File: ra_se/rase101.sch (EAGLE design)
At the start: 32 parts, among them IC1 74HC14D, IC2 24LC08BSN, X1 MAB5WH, X12 LED_01, X2 22-23-2041, X3 MAB5WH

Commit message: ra_se evolve
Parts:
- removed R10: 3k3, rcl:R-EU_M1206
- removed X5, X6: (no value), con-molex:KK-156-3
- added R11: 10k, rcl:R-EU_M1206
- X4: device con-molex:KK-156-3 -> con-molex:KK-156-2
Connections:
- net BTTN_GLOBALSTART renamed BTTN_03
- net BTTN_START_REQST renamed BTTN_01
- net BTTN_STOP_REQST renamed BTTN_02
- net UART1_TX renamed UART1_TX_MAX_I
- removed net INMI_SH: IC1C.O, X5-1.S, X6-1.S
- removed net MAX_O: U$2.RO, X6-3.S
- removed net N$10: U$1.PA10, X6-2.S
- removed net N$11: U$2.DE, U$2.RE, X4-2.S
- removed net N$7: R8.2, X5-2.S
- new net BC2812: IC1A.O, X4-1.S
- new net N$9: IC1A.I, IC1F.O
- new net RS485DIRECT: R11.2, U$1.PB4, U$2.DE, U$2.RE
- new net SPI1_MOSI: IC1F.I, U$1.PA7
- new net UART1_RX_MAX_O: U$1.PA10, U$2.RO
- net +3V3: now also R3.1, R6.1, X2-2.S
- net +5V: now also R11.1; no longer R10.1, R3.1, R6.1, X2-2.S, X4-1.S
- net ENCODER0: now also IC1D.I
- net ENCODER1: now also IC1E.I
- net GND: now also X4-2.S; no longer X4-3.S
- net INMI: now also IC1B.I
- net TIC_RESET: no longer R10.2
- net UART2_RX: now also IC1C.O
- net UART2_TX: now also R8.2; no longer X5-3.S
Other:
- moved on the sheet: IC1A, IC1B, IC1C, IC1D, IC1E, IC1F, IC1P, R3, R6, U$2, X10-1, X10-2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

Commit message: fix
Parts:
- added R10: 10k, rcl:R-EU_M1206
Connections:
- net +5V: now also R10.1
- net UART1_TX_MAX_I: now also R10.2
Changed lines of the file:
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@@
 <part name="GND7" library="supply1" deviceset="GND" device=""/>
 <part name="+3V1" library="supply1" deviceset="+3V3" device=""/>
+<part name="R10" library="rcl" deviceset="R-EU_" device="M1206" value="10k"/>
+<part name="P+2" library="supply1" deviceset="+5V" device=""/>
 </parts>
 <sheets>
@@
 <instance part="GND7" gate="1" x="289.56" y="71.12"/>
 <instance part="+3V1" gate="G$1" x="160.02" y="83.82"/>
+<instance part="R10" gate="G$1" x="109.22" y="101.6" rot="R270"/>
+<instance part="P+2" gate="1" x="109.22" y="111.76"/>
 </instances>
 <busses>
@@
 <segment>
 <pinref part="U$1" gate="G$1" pin="PA10"/>
-<wire x1="76.2" y1="73.66" x2="83.82" y2="73.66" width="0.1524" layer="91"/>
-<label x="83.82" y="73.66" size="1.27" layer="95" xref="yes"/>
+<wire x1="76.2" y1="73.66" x2="81.28" y2="73.66" width="0.1524" layer="91"/>
+<label x="114.3" y="73.66" size="1.27" layer="95" xref="yes"/>
+<wire x1="83.82" y1="73.66" x2="114.3" y2="73.66" width="0.1524" layer="91"/>
+<wire x1="81.28" y1="73.66" x2="83.82" y2="73.66" width="0.1524" layer="91"/>
 </segment>
 </net>
@@
 <pinref part="P+11" gate="1" pin="+5V"/>
 <wire x1="101.6" y1="99.06" x2="101.6" y2="101.6" width="0.1524" layer="91"/>
+</segment>
+<segment>
+<pinref part="P+2" gate="1" pin="+5V"/>
+<pinref part="R10" gate="G$1" pin="1"/>
+<wire x1="109.22" y1="109.22" x2="109.22" y2="106.68" width="0.1524" layer="91"/>
 </segment>
 </net>
@@
 <segment>
 <pinref part="U$1" gate="G$1" pin="PB3"/>
-<wire x1="76.2" y1="83.82" x2="109.22" y2="83.82" width="0.1524" layer="91"/>
-<label x="109.22" y="83.82" size="1.27" layer="95" xref="yes"/>
+<wire x1="76.2" y1="83.82" x2="114.3" y2="83.82" width="0.1524" layer="91"/>
+<label x="114.3" y="83.82" size="1.27" layer="95" xref="yes"/>
 </segment>
 </net>
@@
 <pinref part="R11" gate="G$1" pin="2"/>
 <wire x1="101.6" y1="86.36" x2="101.6" y2="88.9" width="0.1524" layer="91"/>
-<wire x1="101.6" y1="86.36" x2="109.22" y2="86.36" width="0.1524" layer="91"/>
+<wire x1="101.6" y1="86.36" x2="114.3" y2="86.36" width="0.1524" layer="91"/>
 <junction x="101.6" y="86.36"/>
-<label x="109.22" y="86.36" size="1.27" layer="95" xref="yes"/>
+<label x="114.3" y="86.36" size="1.27" layer="95" xref="yes"/>
 </segment>
 <segment>
@@
 <segment>
 <pinref part="U$1" gate="G$1" pin="PA9"/>
-<wire x1="76.2" y1="71.12" x2="83.82" y2="71.12" width="0.1524" layer="91"/>
-<label x="83.82" y="71.12" size="1.27" layer="95" xref="yes"/>
-</segment>
-<segment>
+<wire x1="76.2" y1="71.12" x2="109.22" y2="71.12" width="0.1524" layer="91"/>
+<label x="114.3" y="71.12" size="1.27" layer="95" xref="yes"/>
+<pinref part="R10" gate="G$1" pin="2"/>
+<wire x1="109.22" y1="71.12" x2="114.3" y2="71.12" width="0.1524" layer="91"/>
+<wire x1="109.22" y1="96.52" x2="109.22" y2="71.12" width="0.1524" layer="91"/>
+<junction x="109.22" y="71.12"/>
+</segment>
+<segment>

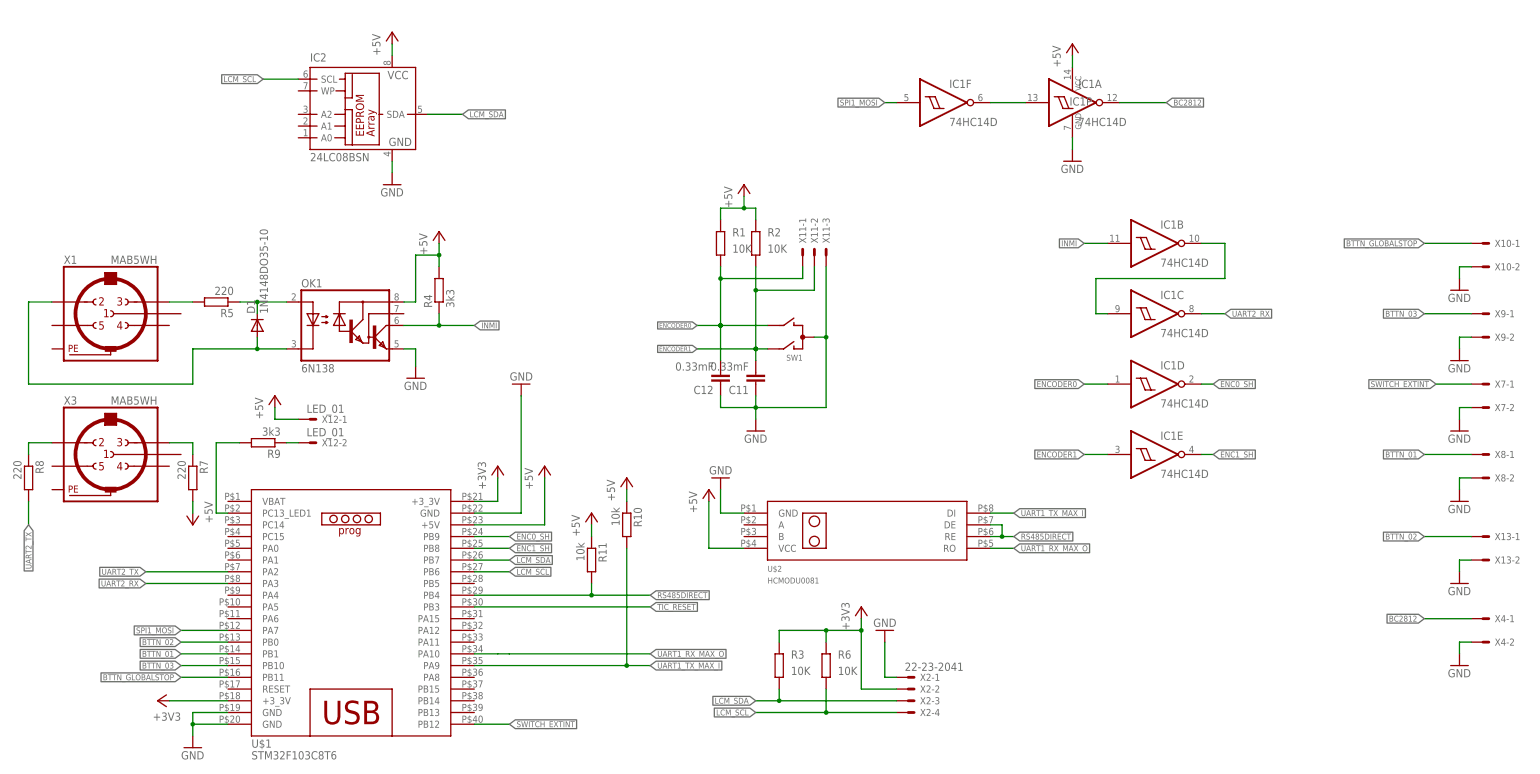
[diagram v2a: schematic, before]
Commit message: oled and other
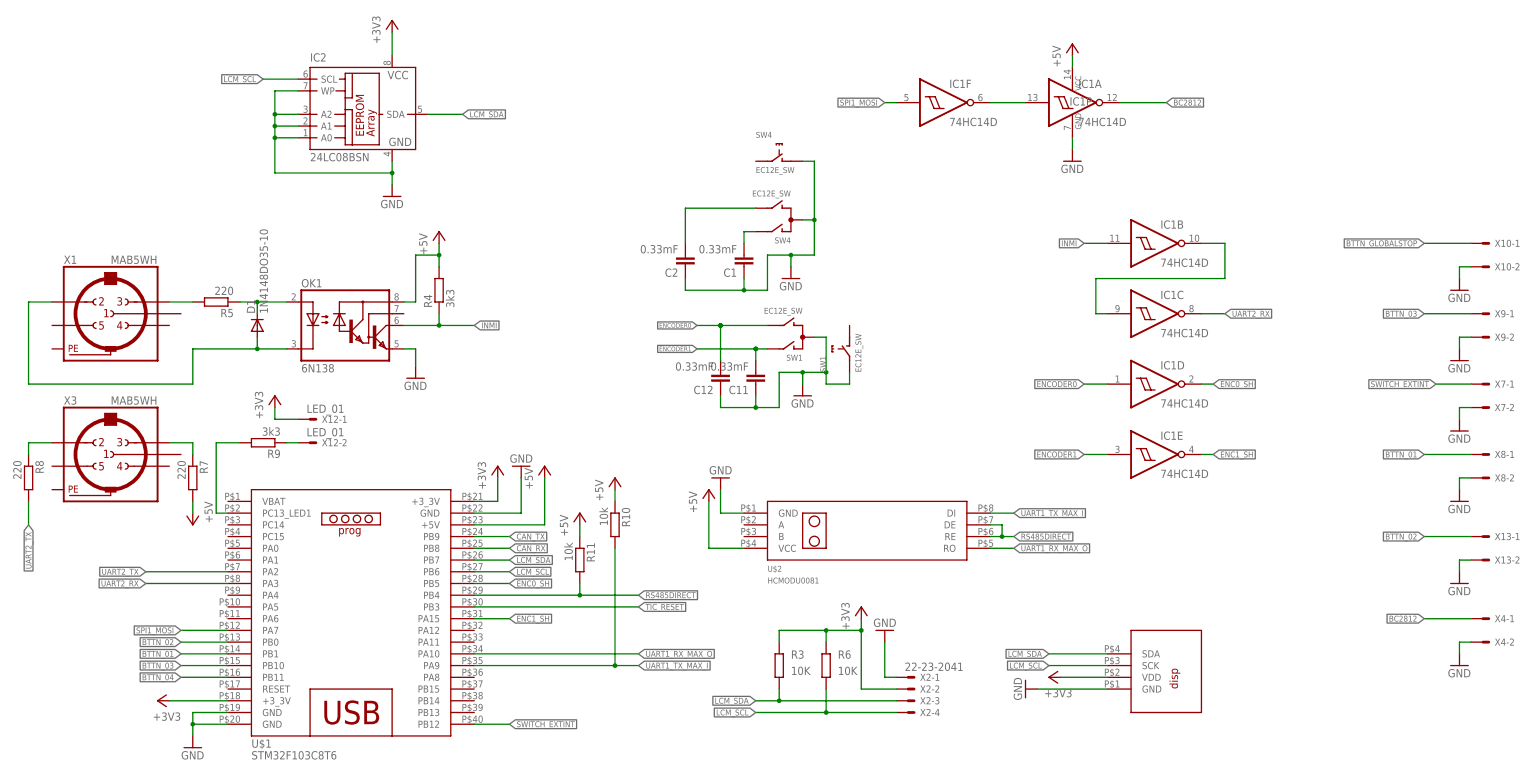
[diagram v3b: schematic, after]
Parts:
- removed R1, R2: 10K, quantum-sensor:R-R1206
- removed X11: (no value), con-molex:KK-156-3
- added C1, C2: 0.33mF, quantum-sensor:C-1206
- added SW4: EC12E_SW, switch-alps:EC12E_SW
- added U$3: OLED_0.96, kolio_oled:OLED_0.96
- SW1: value (none) -> EC12E_SW
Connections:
- new net BTTN_04: U$1.PB11
- new net CAN_RX: U$1.PB8
- new net CAN_TX: U$1.PB9
- new net N$13: C1.2, SW4G$1.A
- new net N$14: C2.2, SW4G$1.B
- net +3V3: now also IC2.VCC, U$3.VDD, X12-1.S
- net +5V: no longer IC2.VCC, R1.1, R2.1, X12-1.S
- net BTTN_GLOBALSTOP: no longer U$1.PB11
- net ENC0_SH: now also U$1.PB5; no longer U$1.PB9
- net ENC1_SH: now also U$1.PA15; no longer U$1.PB8
- net ENCODER0: no longer R1.2, X11-1.S
- net ENCODER1: no longer R2.2, X11-2.S
- net GND: now also C1.1, C2.1, IC2.A0, IC2.A1, IC2.A2, IC2.WP, SW1G$2.2, SW4G$1.C, SW4G$2.1, U$3.GND; no longer X11-3.S
- net LCM_SCL: now also U$3.SCK
- net LCM_SDA: now also U$3.SDA
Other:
- moved on the sheet: R10, R11

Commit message: qq
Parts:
- added R1: 1k, rcl:R-EU_M1206
- R4: value 3k3 -> 470R
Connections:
- new net N$7: OK1.VB, R1.1
- net GND: now also R1.2
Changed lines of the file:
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@@
 <part name="OK1" library="optocoupler" deviceset="6N138" device=""/>
 <part name="GND23" library="supply1" deviceset="GND" device=""/>
-<part name="R4" library="rcl" deviceset="R-EU_" device="M1206" value="3k3"/>
+<part name="R4" library="rcl" deviceset="R-EU_" device="M1206" value="470R"/>
 <part name="D1" library="diode" deviceset="1N4148" device="DO35-10"/>
 <part name="R5" library="rcl" deviceset="R-EU_" device="M1206" value="220"/>
@@
 <part name="GND15" library="supply1" deviceset="GND" device=""/>
 <part name="U$3" library="kolio_oled" deviceset="OLED_0.96" device=""/>
+<part name="R1" library="rcl" deviceset="R-EU_" device="M1206" value="1k"/>
 </parts>
 <sheets>
@@
 <instance part="GND15" gate="1" x="195.58" y="66.04" rot="R270"/>
 <instance part="U$3" gate="G$1" x="231.14" y="68.58" rot="R90"/>
+<instance part="R1" gate="G$1" x="76.2" y="137.16" rot="R180"/>
 </instances>
 <busses>
@@
 <segment>
 <wire x1="60.96" y1="139.7" x2="63.5" y2="139.7" width="0.1524" layer="91"/>
-<wire x1="63.5" y1="139.7" x2="63.5" y2="135.89" width="0.1524" layer="91"/>
+<wire x1="63.5" y1="139.7" x2="63.5" y2="137.16" width="0.1524" layer="91"/>
 <pinref part="OK1" gate="G$1" pin="GND"/>
 <pinref part="GND23" gate="1" pin="GND"/>
+<pinref part="R1" gate="G$1" pin="2"/>
+<wire x1="63.5" y1="137.16" x2="63.5" y2="135.89" width="0.1524" layer="91"/>
+<wire x1="71.12" y1="137.16" x2="63.5" y2="137.16" width="0.1524" layer="91"/>
+<junction x="63.5" y="137.16"/>
 </segment>
 <segment>
@@
 </segment>
 </net>
+<net name="N$7" class="0">
+<segment>
+<pinref part="OK1" gate="G$1" pin="VB"/>
+<wire x1="60.96" y1="147.32" x2="63.5" y2="147.32" width="0.1524" layer="91"/>
+<wire x1="63.5" y1="147.32" x2="63.5" y2="142.24" width="0.1524" layer="91"/>
+<wire x1="63.5" y1="142.24" x2="83.82" y2="142.24" width="0.1524" layer="91"/>
+<wire x1="83.82" y1="142.24" x2="83.82" y2="137.16" width="0.1524" layer="91"/>
+<wire x1="83.82" y1="137.16" x2="81.28" y2="137.16" width="0.1524" layer="91"/>
+<pinref part="R1" gate="G$1" pin="1"/>
+</segment>
+</net>

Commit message: ra_se refactoring
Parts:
- removed C1, C2: 0.33mF, quantum-sensor:C-1206
- removed SW4: EC12E_SW, switch-alps:EC12E_SW
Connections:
- removed net BTTN_04: U$1.PB11
- removed net N$13: C1.2, SW4G$1.A
- removed net N$14: C2.2, SW4G$1.B
- removed net UART2_RX: IC1C.O, U$1.PA3
- removed net UART2_TX: R8.2, U$1.PA2
- new net MISO2: U$1.PB14
- new net MOSI2: U$1.PB15
- new net SCK2: U$1.PB13
- new net SPI1_MISO: U$1.PA6
- new net SPI1_SCK: U$1.PA5
- new net UART3_RX: IC1C.O
- new net UART3_TX: R8.2
- new net USB+: U$1.PA12
- new net USB-: U$1.PA11
- net BTTN_03: no longer U$1.PB10
- net ENC0_SH: no longer U$1.PB5
- net GND: no longer C1.1, C2.1, SW4G$1.C, SW4G$2.1
- net SWITCH_EXTINT: no longer U$1.PB12
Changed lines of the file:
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@@
 <setting verticaltext="up"/>
 </settings>
-<grid distance="0.1" unitdist="inch" unit="inch" style="lines" multiple="1" display="no" altdistance="0.01" altunitdist="inch" altunit="inch"/>
+<grid distance="0.1" unitdist="inch" unit="inch" style="lines" multiple="1" display="yes" altdistance="0.01" altunitdist="inch" altunit="inch"/>
 <layers>
 <layer number="1" name="Top" color="4" fill="1" visible="no" active="no"/>
@@
 <part name="R10" library="rcl" deviceset="R-EU_" device="M1206" value="10k"/>
 <part name="P+2" library="supply1" deviceset="+5V" device=""/>
-<part name="SW4" library="switch-alps" deviceset="EC12E_SW" device=""/>
-<part name="C1" library="quantum-sensor" deviceset="C" device="-1206" value="0.33mF"/>
-<part name="C2" library="quantum-sensor" deviceset="C" device="-1206" value="0.33mF"/>
-<part name="GND14" library="supply1" deviceset="GND" device=""/>
 <part name="+3V4" library="supply1" deviceset="+3V3" device=""/>
 <part name="+3V5" library="supply1" deviceset="+3V3" device=""/>
@@
 <instance part="R10" gate="G$1" x="106.68" y="101.6" rot="R270"/>
 <instance part="P+2" gate="1" x="106.68" y="111.76"/>
-<instance part="SW4" gate="G$1" x="144.78" y="167.64" rot="R90"/>
-<instance part="SW4" gate="G$2" x="142.24" y="180.34"/>
-<instance part="C1" gate="G$1" x="134.62" y="157.48" rot="R180"/>
-<instance part="C2" gate="G$1" x="121.92" y="157.48" rot="R180"/>
-<instance part="GND14" gate="1" x="144.78" y="154.94"/>
 <instance part="+3V4" gate="G$1" x="58.42" y="210.82"/>
 <instance part="SW1" gate="G$2" x="157.48" y="139.7" rot="R90"/>
@@
 </segment>
 <segment>
-<pinref part="SW4" gate="G$1" pin="C"/>
-<wire x1="147.32" y1="167.64" x2="149.86" y2="167.64" width="0.1524" layer="91"/>
-<wire x1="149.86" y1="167.64" x2="149.86" y2="160.02" width="0.1524" layer="91"/>
-<pinref part="GND14" gate="1" pin="GND"/>
-<wire x1="149.86" y1="160.02" x2="144.78" y2="160.02" width="0.1524" layer="91"/>
-<wire x1="144.78" y1="160.02" x2="144.78" y2="157.48" width="0.1524" layer="91"/>
-<pinref part="C1" gate="G$1" pin="1"/>
-<wire x1="134.62" y1="154.94" x2="134.62" y2="152.4" width="0.1524" layer="91"/>
-<wire x1="134.62" y1="152.4" x2="139.7" y2="152.4" width="0.1524" layer="91"/>
-<wire x1="139.7" y1="152.4" x2="139.7" y2="160.02" width="0.1524" layer="91"/>
-<wire x1="139.7" y1="160.02" x2="144.78" y2="160.02" width="0.1524" layer="91"/>
-<junction x="144.78" y="160.02"/>
-<pinref part="C2" gate="G$1" pin="1"/>
-<wire x1="121.92" y1="154.94" x2="121.92" y2="152.4" width="0.1524" layer="91"/>
-<wire x1="121.92" y1="152.4" x2="134.62" y2="152.4" width="0.1524" layer="91"/>
-<junction x="134.62" y="152.4"/>
-<pinref part="SW4" gate="G$2" pin="1"/>
-<wire x1="147.32" y1="180.34" x2="149.86" y2="180.34" width="0.1524" layer="91"/>
-<wire x1="149.86" y1="180.34" x2="149.86" y2="167.64" width="0.1524" layer="91"/>
-<junction x="149.86" y="167.64"/>
-</segment>
-<segment>
 <pinref part="C11" gate="G$1" pin="1"/>
 <wire x1="137.16" y1="129.54" x2="137.16" y2="127" width="0.1524" layer="91"/>
@@
 </segment>
 </net>
-<net name="UART2_TX" class="0">
-<segment>
-<pinref part="U$1" gate="G$1" pin="PA2"/>
-<wire x1="22.86" y1="91.44" x2="5.08" y2="91.44" width="0.1524" layer="91"/>
-<label x="5.08" y="91.44" size="1.27" layer="95" rot="R180" xref="yes"/>
-</segment>
+<net name="UART3_TX" class="0">
 <segment>
 <pinref part="R8" gate="G$1" pin="2"/>
@@
 <label x="-20.32" y="101.6" size="1.27" layer="95" rot="R270" xref="yes"/>
 </segment>
+<segment>
+<wire x1="22.86" y1="71.12" x2="5.08" y2="71.12" width="0.1524" layer="91"/>
+<label x="5.08" y="71.12" size="1.27" layer="95" rot="R180" xref="yes"/>
+</segment>
 </net>
 <net name="BTTN_03" class="0">
-<segment>
-<pinref part="U$1" gate="G$1" pin="PB10"/>
-<wire x1="22.86" y1="71.12" x2="12.7" y2="71.12" width="0.1524" layer="91"/>
-<label x="12.7" y="71.12" size="1.27" layer="95" rot="R180" xref="yes"/>
-</segment>
 <segment>
 <wire x1="292.1" y1="147.32" x2="281.94" y2="147.32" width="0.1524" layer="91"/>
 <label x="281.94" y="147.32" size="1.27" layer="95" rot="R180" xref="yes"/>
 <pinref part="X9" gate="-1" pin="S"/>
+</segment>
+<segment>
+<wire x1="22.86" y1="93.98" x2="5.08" y2="93.98" width="0.1524" layer="91"/>
+<label x="5.08" y="93.98" size="1.27" layer="95" rot="R180" xref="yes"/>
 </segment>
 </net>
@@
 <net name="SWITCH_EXTINT" class="0">
 <segment>
-<pinref part="U$1" gate="G$1" pin="PB12"/>
-<wire x1="76.2" y1="58.42" x2="83.82" y2="58.42" width="0.1524" layer="91"/>
-<label x="83.82" y="58.42" size="1.27" layer="95" xref="yes"/>
-</segment>
-<segment>
 <wire x1="284.48" y1="132.08" x2="292.1" y2="132.08" width="0.1524" layer="91"/>
 <label x="284.48" y="132.08" size="1.27" layer="95" rot="R180" xref="yes"/>
 <pinref part="X7" gate="-1" pin="S"/>
+</segment>
+<segment>
+<wire x1="76.2" y1="88.9" x2="83.82" y2="88.9" width="0.1524" layer="91"/>
+<label x="83.82" y="88.9" size="1.27" layer="95" xref="yes"/>
 </segment>
 </net>
@@
 </segment>
 <segment>
-<wire x1="76.2" y1="88.9" x2="83.82" y2="88.9" width="0.1524" layer="91"/>
-<pinref part="U$1" gate="G$1" pin="PB5"/>
-<label x="83.82" y="88.9" size="1.27" layer="95" xref="yes"/>
+<wire x1="76.2" y1="58.42" x2="83.82" y2="58.42" width="0.1524" layer="91"/>
+<label x="83.82" y="58.42" size="1.27" layer="95" xref="yes"/>
 </segment>
 </net>
@@
 <label x="281.94" y="99.06" size="1.27" layer="95" rot="R180" xref="yes"/>
 <pinref part="X13" gate="-1" pin="S"/>
-</segment>
-</net>
-<net name="UART2_RX" class="0">
-<segment>
-<pinref part="U$1" gate="G$1" pin="PA3"/>
-<wire x1="22.86" y1="88.9" x2="5.08" y2="88.9" width="0.1524" layer="91"/>
-<label x="5.08" y="88.9" size="1.27" layer="95" rot="R180" xref="yes"/>
-</segment>
-<segment>
-<pinref part="IC1" gate="C" pin="O"/>
-<label x="238.76" y="147.32" size="1.27" layer="95" xref="yes"/>
-<wire x1="233.68" y1="147.32" x2="238.76" y2="147.32" width="0.1524" layer="91"/>
 </segment>
 </net>
@@
 </segment>
 </net>
-<net name="N$13" class="0">
-<segment>
-<pinref part="C1" gate="G$1" pin="2"/>
-<wire x1="134.62" y1="162.56" x2="134.62" y2="165.1" width="0.1524" layer="91"/>
-<pinref part="SW4" gate="G$1" pin="A"/>
-<wire x1="134.62" y1="165.1" x2="137.16" y2="165.1" width="0.1524" layer="91"/>
-</segment>
-</net>
-<net name="N$14" class="0">
-<segment>
-<pinref part="C2" gate="G$1" pin="2"/>
-<wire x1="121.92" y1="162.56" x2="121.92" y2="170.18" width="0.1524" layer="91"/>
-<pinref part="SW4" gate="G$1" pin="B"/>
-<wire x1="121.92" y1="170.18" x2="137.16" y2="170.18" width="0.1524" layer="91"/>
-</segment>
-</net>
 <net name="CAN_TX" class="0">
 <segment>
@@
 <label x="83.82" y="96.52" size="1.27" layer="95" xref="yes"/>
 <pinref part="U$1" gate="G$1" pin="PB8"/>
-</segment>
-</net>
-<net name="BTTN_04" class="0">
-<segment>
-<pinref part="U$1" gate="G$1" pin="PB11"/>
-<wire x1="22.86" y1="68.58" x2="12.7" y2="68.58" width="0.1524" layer="91"/>
-<label x="12.7" y="68.58" size="1.27" layer="95" rot="R180" xref="yes"/>
 </segment>
 </net>
@@
 </segment>
 </net>
+<net name="USB+" class="0">
+<segment>
+<pinref part="U$1" gate="G$1" pin="PA12"/>
+<wire x1="76.2" y1="78.74" x2="83.82" y2="78.74" width="0.1524" layer="91"/>
+<label x="83.82" y="78.74" size="1.27" layer="95" xref="yes"/>
+</segment>
+</net>
+<net name="USB-" class="0">
+<segment>
+<pinref part="U$1" gate="G$1" pin="PA11"/>
+<wire x1="76.2" y1="76.2" x2="83.82" y2="76.2" width="0.1524" layer="91"/>
+<label x="83.82" y="76.2" size="1.27" layer="95" xref="yes"/>
+</segment>
+</net>
+<net name="BTTN_04" class="0">
+<segment>
+<wire x1="22.86" y1="86.36" x2="5.08" y2="86.36" width="0.1524" layer="91"/>
+<label x="5.08" y="86.36" size="1.27" layer="95" rot="R180" xref="yes"/>
+</segment>
+</net>
+<net name="SPI1_SCK" class="0">
+<segment>
+<pinref part="U$1" gate="G$1" pin="PA5"/>
+<wire x1="22.86" y1="83.82" x2="12.7" y2="83.82" width="0.1524" layer="91"/>
+<label x="12.7" y="83.82" size="1.27" layer="95" rot="R180" xref="yes"/>
+</segment>
+</net>
+<net name="SPI1_MISO" class="0">
+<segment>
+<pinref part="U$1" gate="G$1" pin="PA6"/>
+<wire x1="22.86" y1="81.28" x2="12.7" y2="81.28" width="0.1524" layer="91"/>
+<label x="12.7" y="81.28" size="1.27" layer="95" rot="R180" xref="yes"/>
+</segment>
+</net>
+<net name="UART3_RX" class="0">
+<segment>
+<wire x1="22.86" y1="68.58" x2="5.08" y2="68.58" width="0.1524" layer="91"/>
+<label x="5.08" y="68.58" size="1.27" layer="95" rot="R180" xref="yes"/>
+</segment>
+<segment>
+<pinref part="IC1" gate="C" pin="O"/>
+<label x="238.76" y="147.32" size="1.27" layer="95" xref="yes"/>
+<wire x1="233.68" y1="147.32" x2="238.76" y2="147.32" width="0.1524" layer="91"/>
+</segment>
+</net>
+<net name="SCK2" class="0">
+<segment>
+<pinref part="U$1" gate="G$1" pin="PB13"/>
+<wire x1="76.2" y1="60.96" x2="83.82" y2="60.96" width="0.1524" layer="91"/>
+<label x="83.82" y="60.96" size="1.27" layer="95" xref="yes"/>
+</segment>
+</net>
+<net name="MISO2" class="0">
+<segment>
+<pinref part="U$1" gate="G$1" pin="PB14"/>
+<wire x1="76.2" y1="63.5" x2="83.82" y2="63.5" width="0.1524" layer="91"/>
+<label x="83.82" y="63.5" size="1.27" layer="95" xref="yes"/>
+</segment>
+</net>
+<net name="MOSI2" class="0">
+<segment>
+<pinref part="U$1" gate="G$1" pin="PB15"/>
+<wire x1="76.2" y1="66.04" x2="83.82" y2="66.04" width="0.1524" layer="91"/>
+<label x="83.82" y="66.04" size="1.27" layer="95" xref="yes"/>
+</segment>
+</net>
